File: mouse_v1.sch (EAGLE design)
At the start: 62 parts, among them U1 L293DD, X1 22-23-2021, X2 22-23-2021

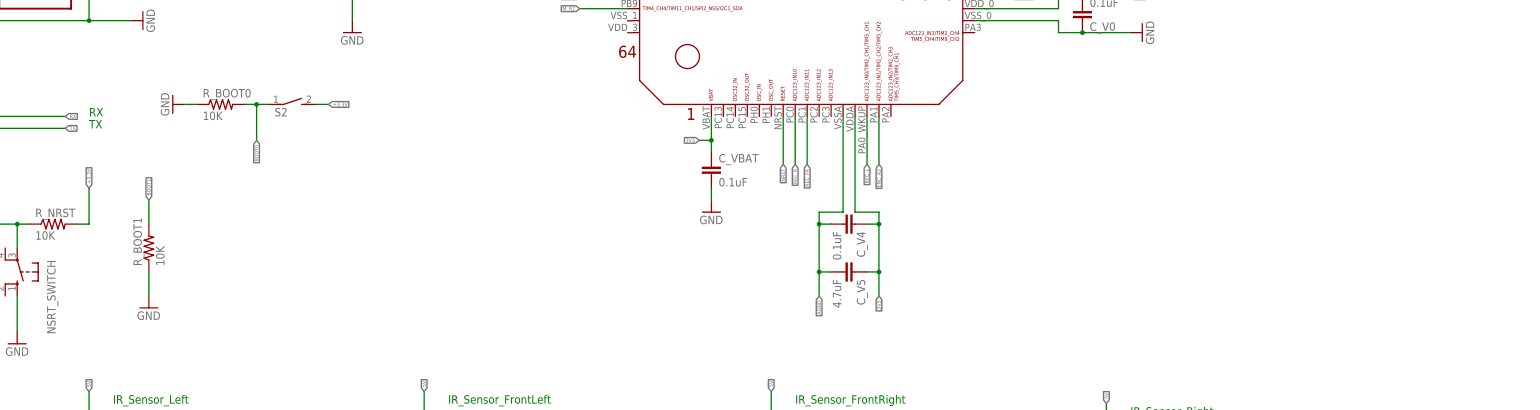
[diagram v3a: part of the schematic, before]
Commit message: Created Gyro package
Created gyro (LY3200ALH) library and added it to the schematic. Not wired.
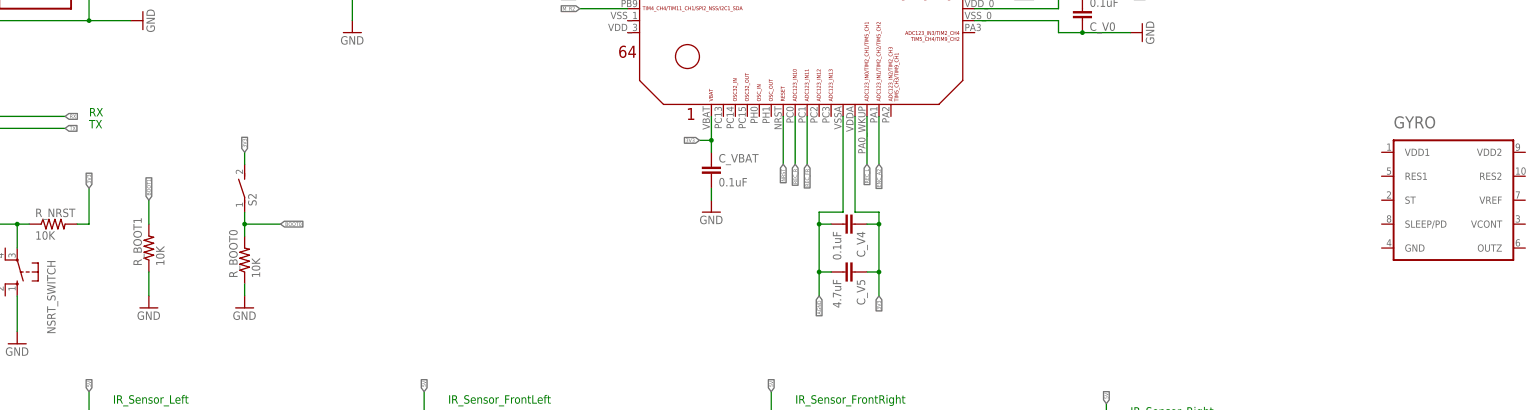
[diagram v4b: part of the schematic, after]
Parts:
- added GYRO: LY3200ALH, LY3200ALH:LY3200ALH
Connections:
- removed net +3.3V: R_NRST.2, S2.2
- net 3V3: now also R_NRST.2, S2.2
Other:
- moved on the sheet: R_BOOT0, S2
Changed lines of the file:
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@@
 <?xml version="1.0" encoding="utf-8"?>
 <!DOCTYPE eagle SYSTEM "eagle.dtd">
-<eagle version="9.2.2">
+<eagle version="8.6.1">
 <drawing>
 <settings>
@@
 <part name="X1" library="con-molex" library_urn="urn:adsk.eagle:library:165" deviceset="22-23-2021" device=""/>
 <part name="X2" library="con-molex" library_urn="urn:adsk.eagle:library:165" deviceset="22-23-2021" device=""/>
+<part name="GYRO" library="LY3200ALH" deviceset="LY3200ALH" device=""/>
 </parts>
 <sheets>
@@
 <attribute name="VALUE" x="-27.94" y="-104.14" size="1.778" layer="96"/>
 </instance>
-<instance part="S2" gate="1" x="5.08" y="-58.42" smashed="yes" rot="R270">
-<attribute name="NAME" x="1.27" y="-60.96" size="1.778" layer="95"/>
-<attribute name="VALUE" x="1.27" y="-63.5" size="1.778" layer="96"/>
-</instance>
-<instance part="R_BOOT0" gate="G$1" x="-10.16" y="-58.42" smashed="yes">
-<attribute name="NAME" x="-13.97" y="-56.9214" size="1.778" layer="95"/>
-<attribute name="VALUE" x="-13.97" y="-61.722" size="1.778" layer="96"/>
-</instance>
-<instance part="GND19" gate="1" x="-20.32" y="-58.42" smashed="yes" rot="R270">
-<attribute name="VALUE" x="-22.86" y="-55.88" size="1.778" layer="96" rot="R270"/>
+<instance part="S2" gate="1" x="-5.08" y="-76.2" smashed="yes">
+<attribute name="NAME" x="-2.54" y="-80.01" size="1.778" layer="95" rot="R90"/>
+<attribute name="VALUE" x="0" y="-80.01" size="1.778" layer="96" rot="R90"/>
+</instance>
+<instance part="R_BOOT0" gate="G$1" x="-5.08" y="-91.44" smashed="yes" rot="R90">
+<attribute name="NAME" x="-6.5786" y="-95.25" size="1.778" layer="95" rot="R90"/>
+<attribute name="VALUE" x="-1.778" y="-95.25" size="1.778" layer="96" rot="R90"/>
+</instance>
+<instance part="GND19" gate="1" x="-5.08" y="-101.6" smashed="yes">
+<attribute name="VALUE" x="-7.62" y="-104.14" size="1.778" layer="96"/>
 </instance>
 <instance part="X1" gate="-1" x="182.88" y="50.8" smashed="yes">
@@
 <attribute name="NAME" x="185.42" y="42.418" size="1.524" layer="95"/>
 </instance>
+<instance part="GYRO" gate="G$1" x="251.46" y="-78.74"/>
 </instances>
 <busses>
@@
 <segment>
 <pinref part="R_BOOT0" gate="G$1" pin="1"/>
-<wire x1="-15.24" y1="-58.42" x2="-17.78" y2="-58.42" width="0.1524" layer="91"/>
+<wire x1="-5.08" y1="-96.52" x2="-5.08" y2="-99.06" width="0.1524" layer="91"/>
 <pinref part="GND19" gate="1" pin="GND"/>
 </segment>
@@
 <label x="129.54" y="-99.06" size="0.8128" layer="95" rot="R270" xref="yes"/>
 </segment>
+<segment>
+<pinref part="R_NRST" gate="G$1" pin="2"/>
+<wire x1="-40.64" y1="-83.82" x2="-38.1" y2="-83.82" width="0.1524" layer="91"/>
+<wire x1="-38.1" y1="-83.82" x2="-38.1" y2="-76.2" width="0.1524" layer="91"/>
+<label x="-38.1" y="-76.2" size="0.8128" layer="95" rot="R90" xref="yes"/>
+</segment>
+<segment>
+<pinref part="S2" gate="1" pin="2"/>
+<wire x1="-5.08" y1="-71.12" x2="-5.08" y2="-68.58" width="0.1524" layer="91"/>
+<label x="-5.08" y="-68.58" size="0.8128" layer="95" rot="R90" xref="yes"/>
+</segment>
 </net>
 <net name="AGND" class="0">
@@
 <segment>
 <pinref part="S2" gate="1" pin="1"/>
-<wire x1="0" y1="-58.42" x2="-2.54" y2="-58.42" width="0.1524" layer="91"/>
-<junction x="-2.54" y="-58.42"/>
-<wire x1="-2.54" y1="-58.42" x2="-2.54" y2="-66.04" width="0.1524" layer="91"/>
-<label x="-2.54" y="-66.04" size="0.8128" layer="95" rot="R270" xref="yes"/>
-<wire x1="-2.54" y1="-58.42" x2="-5.08" y2="-58.42" width="0.1524" layer="91"/>
+<wire x1="-5.08" y1="-81.28" x2="-5.08" y2="-83.82" width="0.1524" layer="91"/>
+<junction x="-5.08" y="-83.82"/>
+<wire x1="-5.08" y1="-83.82" x2="2.54" y2="-83.82" width="0.1524" layer="91"/>
+<label x="2.54" y="-83.82" size="0.8128" layer="95" xref="yes"/>
+<wire x1="-5.08" y1="-83.82" x2="-5.08" y2="-86.36" width="0.1524" layer="91"/>
 <pinref part="R_BOOT0" gate="G$1" pin="2"/>
 </segment>
@@
 </segment>
 </net>
-<net name="+3.3V" class="0">
-<segment>
-<pinref part="R_NRST" gate="G$1" pin="2"/>
-<wire x1="-40.64" y1="-83.82" x2="-38.1" y2="-83.82" width="0.1524" layer="91"/>
-<wire x1="-38.1" y1="-83.82" x2="-38.1" y2="-76.2" width="0.1524" layer="91"/>
-<label x="-38.1" y="-76.2" size="0.8128" layer="95" rot="R90" xref="yes"/>
-</segment>
-<segment>
-<pinref part="S2" gate="1" pin="2"/>
-<wire x1="10.16" y1="-58.42" x2="12.7" y2="-58.42" width="0.1524" layer="91"/>
-<label x="12.7" y="-58.42" size="0.8128" layer="95" xref="yes"/>
-</segment>
-</net>

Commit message: Added Gyro and Pin headers
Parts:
- removed X1, X2: 22-23-2021, con-molex:22-23-2021
- added C1: 470nF, capacitor-wima:C2,5-3
- added C2: 10nF, capacitor-wima:C2,5-3
- added PIN_HEADERS: (no value), con-lstb:MA04-2
- added R1: 10K, rcl:R-US_0204/2V
- renumbered NSRT_SWITCH to NRST_SWITCH
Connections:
- removed net NSRT: NRST_SWITCH.P, R_NRST.1
- new net 3.3V: GYRO.VDD1, GYRO.VDD2, PIN_HEADERS.1
- new net GYRO: GYRO.OUTZ, U$1.PC5
- new net N$5: C1.2, R1.1
- new net N$9: C1.1, C2.1, GYRO.VCONT
- net GND: now also C2.2, GYRO.GND, PIN_HEADERS.3, PIN_HEADERS.6, R1.2; no longer X2-2.S
- net NRST: now also NRST_SWITCH.P, PIN_HEADERS.2, R_NRST.1; no longer X2-1.S
- net RX: now also PIN_HEADERS.5
- net SWCLK: now also PIN_HEADERS.8; no longer X1-1.S
- net SWDIO: now also PIN_HEADERS.4; no longer X1-2.S
- net TX: now also PIN_HEADERS.7
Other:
- moved on the sheet: GYRO

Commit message: More LEDs
Added green and red LED for debugging. Red is programmable, green tells if mouse is powered.
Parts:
- removed LED: (no value), led:LEDCHIPLED_0603
- removed R_LED: 100, SparkFun-Resistors:1.8KOHM1/10W1%(0603)
- added LED1: BLUE, led:LEDCHIPLED_0603
- added LED2: RED, led:LEDCHIPLED_0603
- added LED3: GREEN, led:LEDCHIPLED_0603
- added R_LED1: 100, SparkFun-Resistors:1.8KOHM1/10W1%(0603)
- added R_LED2, R_LED3: 330, SparkFun-Resistors:1.8KOHM1/10W1%(0603)
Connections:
- removed net LED: R_LED.2, U$1.PB12
- new net LED1: R_LED1.2, U$1.PB12
- new net LED2: R_LED2.2, U$1.PB13
- new net N$10: LED2.A, R_LED2.1
- new net N$11: LED3.A, R_LED3.1
- net 3V3: now also R_LED3.2
- net GND: now also LED1.C, LED2.C, LED3.C; no longer LED.C
- net N$8: now also LED1.A, R_LED1.1; no longer LED.A, R_LED.1
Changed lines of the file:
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@@
 <?xml version="1.0" encoding="utf-8"?>
 <!DOCTYPE eagle SYSTEM "eagle.dtd">
-<eagle version="9.2.2">
+<eagle version="8.6.1">
 <drawing>
 <settings>
@@
 <part name="C_3V3REG2" library="SparkFun" deviceset="CAP" device="0603-CAP" value="0.1uF"/>
 <part name="U1" library="L293DD" deviceset="L293DD" device=""/>
-<part name="R_LED" library="SparkFun-Resistors" deviceset="1.8KOHM1/10W1%(0603)" device="" value="100"/>
-<part name="LED" library="led" library_urn="urn:adsk.eagle:library:259" deviceset="LED" device="CHIPLED_0603" package3d_urn="urn:adsk.eagle:package:15822/2"/>
+<part name="R_LED1" library="SparkFun-Resistors" deviceset="1.8KOHM1/10W1%(0603)" device="" value="100"/>
+<part name="LED1" library="led" library_urn="urn:adsk.eagle:library:259" deviceset="LED" device="CHIPLED_0603" package3d_urn="urn:adsk.eagle:package:15822/2" value="BLUE"/>
 <part name="GND4" library="SparkFun" deviceset="GND" device=""/>
 <part name="T_IR-L" library="MMBF170LT1" deviceset="MMBF170LT1G" device=""/>
@@
 <part name="R1" library="rcl" library_urn="urn:adsk.eagle:library:334" deviceset="R-US_" device="0204/2V" package3d_urn="urn:adsk.eagle:package:23495/1" value="10K"/>
 <part name="GND21" library="supply1" library_urn="urn:adsk.eagle:library:371" deviceset="GND" device=""/>
+<part name="R_LED2" library="SparkFun-Resistors" deviceset="1.8KOHM1/10W1%(0603)" device="" value="330"/>
+<part name="LED2" library="led" library_urn="urn:adsk.eagle:library:259" deviceset="LED" device="CHIPLED_0603" package3d_urn="urn:adsk.eagle:package:15822/2" value="RED"/>
+<part name="GND22" library="SparkFun" deviceset="GND" device=""/>
+<part name="R_LED3" library="SparkFun-Resistors" deviceset="1.8KOHM1/10W1%(0603)" device="" value="330"/>
+<part name="LED3" library="led" library_urn="urn:adsk.eagle:library:259" deviceset="LED" device="CHIPLED_0603" package3d_urn="urn:adsk.eagle:package:15822/2" value="GREEN"/>
+<part name="GND23" library="SparkFun" deviceset="GND" device=""/>
 </parts>
 <sheets>
@@
 <attribute name="VALUE" x="-43.4594" y="62.4586" size="2.0828" layer="96" ratio="6" rot="SR0"/>
 </instance>
-<instance part="R_LED" gate="G$1" x="17.78" y="-17.78" smashed="yes" rot="R90">
-<attribute name="NAME" x="16.2814" y="-21.59" size="1.778" layer="95" rot="R90"/>
-<attribute name="VALUE" x="21.082" y="-21.59" size="1.778" layer="96" rot="R90"/>
-</instance>
-<instance part="LED" gate="G$1" x="17.78" y="-30.48" smashed="yes">
-<attribute name="NAME" x="21.336" y="-35.052" size="1.778" layer="95" rot="R90"/>
-<attribute name="VALUE" x="23.495" y="-35.052" size="1.778" layer="96" rot="R90"/>
-</instance>
-<instance part="GND4" gate="1" x="17.78" y="-43.18" smashed="yes">
-<attribute name="VALUE" x="15.24" y="-45.72" size="1.778" layer="96"/>
+<instance part="R_LED1" gate="G$1" x="2.54" y="-17.78" smashed="yes" rot="R90">
+<attribute name="NAME" x="1.0414" y="-21.59" size="1.778" layer="95" rot="R90"/>
+<attribute name="VALUE" x="5.842" y="-21.59" size="1.778" layer="96" rot="R90"/>
+</instance>
+<instance part="LED1" gate="G$1" x="2.54" y="-30.48" smashed="yes">
+<attribute name="NAME" x="6.096" y="-35.052" size="1.778" layer="95" rot="R90"/>
+<attribute name="VALUE" x="8.255" y="-35.052" size="1.778" layer="96" rot="R90"/>
+</instance>
+<instance part="GND4" gate="1" x="2.54" y="-43.18" smashed="yes">
+<attribute name="VALUE" x="0" y="-45.72" size="1.778" layer="96"/>
 </instance>
 <instance part="T_IR-L" gate="A" x="-40.64" y="-165.1" smashed="yes">
@@
 <instance part="GND21" gate="1" x="271.78" y="-81.28" smashed="yes" rot="R90">
 <attribute name="VALUE" x="274.32" y="-83.82" size="1.778" layer="96" rot="R90"/>
+</instance>
+<instance part="R_LED2" gate="G$1" x="15.24" y="-17.78" smashed="yes" rot="R90">
+<attribute name="NAME" x="13.7414" y="-21.59" size="1.778" layer="95" rot="R90"/>
+<attribute name="VALUE" x="18.542" y="-21.59" size="1.778" layer="96" rot="R90"/>
+</instance>
+<instance part="LED2" gate="G$1" x="15.24" y="-30.48" smashed="yes">
+<attribute name="NAME" x="18.796" y="-35.052" size="1.778" layer="95" rot="R90"/>
+<attribute name="VALUE" x="20.955" y="-35.052" size="1.778" layer="96" rot="R90"/>
+</instance>
+<instance part="GND22" gate="1" x="15.24" y="-43.18" smashed="yes">
+<attribute name="VALUE" x="12.7" y="-45.72" size="1.778" layer="96"/>
+</instance>
+<instance part="R_LED3" gate="G$1" x="27.94" y="-17.78" smashed="yes" rot="R90">
+<attribute name="NAME" x="26.4414" y="-21.59" size="1.778" layer="95" rot="R90"/>
+<attribute name="VALUE" x="31.242" y="-21.59" size="1.778" layer="96" rot="R90"/>
+</instance>
+<instance part="LED3" gate="G$1" x="27.94" y="-30.48" smashed="yes">
+<attribute name="NAME" x="31.496" y="-35.052" size="1.778" layer="95" rot="R90"/>
+<attribute name="VALUE" x="33.655" y="-35.052" size="1.778" layer="96" rot="R90"/>
+</instance>
+<instance part="GND23" gate="1" x="27.94" y="-43.18" smashed="yes">
+<attribute name="VALUE" x="25.4" y="-45.72" size="1.778" layer="96"/>
 </instance>
 </instances>
@@
 </segment>
 <segment>
-<pinref part="LED" gate="G$1" pin="C"/>
+<pinref part="LED1" gate="G$1" pin="C"/>
 <pinref part="GND4" gate="1" pin="GND"/>
-<wire x1="17.78" y1="-35.56" x2="17.78" y2="-40.64" width="0.1524" layer="91"/>
+<wire x1="2.54" y1="-35.56" x2="2.54" y2="-40.64" width="0.1524" layer="91"/>
 </segment>
 <segment>
@@
 <wire x1="266.7" y1="-81.28" x2="269.24" y2="-81.28" width="0.1524" layer="91"/>
 <pinref part="GND21" gate="1" pin="GND"/>
+</segment>
+<segment>
+<pinref part="LED2" gate="G$1" pin="C"/>
+<pinref part="GND22" gate="1" pin="GND"/>
+<wire x1="15.24" y1="-35.56" x2="15.24" y2="-40.64" width="0.1524" layer="91"/>
+</segment>
+<segment>
+<pinref part="LED3" gate="G$1" pin="C"/>
+<pinref part="GND23" gate="1" pin="GND"/>
+<wire x1="27.94" y1="-35.56" x2="27.94" y2="-40.64" width="0.1524" layer="91"/>
 </segment>
 </net>
@@
 <wire x1="-5.08" y1="-71.12" x2="-5.08" y2="-68.58" width="0.1524" layer="91"/>
 <label x="-5.08" y="-68.58" size="0.8128" layer="95" rot="R90" xref="yes"/>
+</segment>
+<segment>
+<pinref part="R_LED3" gate="G$1" pin="2"/>
+<wire x1="27.94" y1="-12.7" x2="27.94" y2="-7.62" width="0.1524" layer="91"/>
+<label x="27.94" y="-7.62" size="0.8128" layer="95" rot="R90" xref="yes"/>
 </segment>
 </net>
@@
 </segment>
 </net>
-<net name="LED" class="0">
-<segment>
-<pinref part="U$1" gate="G$1" pin="PB12"/>
-<wire x1="132.08" y1="12.7" x2="132.08" y2="22.86" width="0.1524" layer="91"/>
-<label x="132.08" y="22.86" size="0.8128" layer="95" rot="R90" xref="yes"/>
-</segment>
-<segment>
-<pinref part="R_LED" gate="G$1" pin="2"/>
-<wire x1="17.78" y1="-12.7" x2="17.78" y2="-7.62" width="0.1524" layer="91"/>
-<label x="17.78" y="-7.62" size="0.8128" layer="95" rot="R90" xref="yes"/>
-</segment>
-</net>
 <net name="N$8" class="0">
 <segment>
-<pinref part="R_LED" gate="G$1" pin="1"/>
-<pinref part="LED" gate="G$1" pin="A"/>
-<wire x1="17.78" y1="-22.86" x2="17.78" y2="-27.94" width="0.1524" layer="91"/>
+<pinref part="R_LED1" gate="G$1" pin="1"/>
+<pinref part="LED1" gate="G$1" pin="A"/>
+<wire x1="2.54" y1="-22.86" x2="2.54" y2="-27.94" width="0.1524" layer="91"/>
 </segment>
 </net>
@@
 </segment>
 </net>
+<net name="N$10" class="0">
+<segment>
+<pinref part="R_LED2" gate="G$1" pin="1"/>
+<pinref part="LED2" gate="G$1" pin="A"/>
+<wire x1="15.24" y1="-22.86" x2="15.24" y2="-27.94" width="0.1524" layer="91"/>
+</segment>
+</net>
+<net name="N$11" class="0">
+<segment>
+<pinref part="R_LED3" gate="G$1" pin="1"/>
+<pinref part="LED3" gate="G$1" pin="A"/>
+<wire x1="27.94" y1="-22.86" x2="27.94" y2="-27.94" width="0.1524" layer="91"/>
+</segment>
+</net>
+<net name="LED2" class="0">
+<segment>
+<pinref part="U$1" gate="G$1" pin="PB13"/>
+<wire x1="129.54" y1="12.7" x2="129.54" y2="22.86" width="0.1524" layer="91"/>
+<label x="129.54" y="22.86" size="0.8128" layer="95" rot="R90" xref="yes"/>
+</segment>
+<segment>
+<pinref part="R_LED2" gate="G$1" pin="2"/>
+<wire x1="15.24" y1="-12.7" x2="15.24" y2="-7.62" width="0.1524" layer="91"/>
+<label x="15.24" y="-7.62" size="0.8128" layer="95" rot="R90" xref="yes"/>
+</segment>
+</net>
+<net name="LED1" class="0">
+<segment>
+<pinref part="U$1" gate="G$1" pin="PB12"/>
+<wire x1="132.08" y1="12.7" x2="132.08" y2="22.86" width="0.1524" layer="91"/>
+<label x="132.08" y="22.86" size="0.8128" layer="95" rot="R90" xref="yes"/>
+</segment>
+<segment>
+<pinref part="R_LED1" gate="G$1" pin="2"/>
+<wire x1="2.54" y1="-12.7" x2="2.54" y2="-7.62" width="0.1524" layer="91"/>
+<label x="2.54" y="-7.62" size="0.8128" layer="95" rot="R90" xref="yes"/>
+</segment>
+</net>

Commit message: ENC_B2 pin change
Changed from PC4 -> PA3. PC4 is an ADC pin while we need a PWM (TIM) pin for the encoders.
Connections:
- removed net M_R1: U$1.PB8
- removed net M_R2: U$1.PB9
- net ENC_B2: now also U$1.PA3; no longer U$1.PC4
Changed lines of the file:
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@@
-</segment>
-</net>
-<net name="M_R1" class="0">
-<segment>
-<pinref part="U$1" gate="G$1" pin="PB8"/>
-<wire x1="76.2" y1="-35.56" x2="66.04" y2="-35.56" width="0.1524" layer="91"/>
-<label x="66.04" y="-35.56" size="0.8128" layer="95" rot="R180" xref="yes"/>
-</segment>
-</net>
-<net name="M_R2" class="0">
-<segment>
-<pinref part="U$1" gate="G$1" pin="PB9"/>
-<wire x1="76.2" y1="-38.1" x2="66.04" y2="-38.1" width="0.1524" layer="91"/>
-<label x="66.04" y="-38.1" size="0.8128" layer="95" rot="R180" xref="yes"/>
 </segment>
 </net>
@@
 </segment>
 <segment>
-<pinref part="U$1" gate="G$1" pin="PC4"/>
-<wire x1="149.86" y1="-25.4" x2="157.48" y2="-25.4" width="0.1524" layer="91"/>
-<label x="157.48" y="-25.4" size="0.8128" layer="95" xref="yes"/>
-</segment>
-</net>
+<pinref part="U$1" gate="G$1" pin="PA3"/>
+<wire x1="149.86" y1="-43.18" x2="157.48" y2="-43.18" width="0.1524" layer="91"/>
+<label x="157.48" y="-43.18" size="0.8128" layer="95" xref="yes"/>
+</segment>
+</net>
